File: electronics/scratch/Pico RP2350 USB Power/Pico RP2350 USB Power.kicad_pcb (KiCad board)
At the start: 2 copper layers, 77 x 64 mm, 48 parts, among them J1 RFM69HCW, J10 IR TX AOE, J11 IR RX 1, J12 IR RX 2, J13 IR RX 3, J14 BUTTON A, J15 BUTTON B, J16 LED STRIP 1, J17 LED STRIP 2, J18 LED STRIP 3, J19 LED STRIP 4, J2 SD CARD, J20 LED STRIP 5, J21 LED STRIP 6, J22 POWER, J3 I2C_1, J4 I2C_2, J5 I2C_3, J6 I2C_STEMMA, J7 I2S AMP, J8 IR TX LINE, J9 IR TX CONE, Q1 AO3406, Q2 AO3406, Q3 AO3406, Q4 AO3401A, Q5 C20917, SW1 POWER, U1 74HCT244

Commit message: More pinout labels, removed some component labels, fixed STEMMA MP ground.
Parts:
- J6: value I2C_STEMMA -> STEMMA
- moved J13 3.46 mm to (138.0, 101.0)
- moved J12 2.08 mm to (127.9, 101.0)
- moved J5 2.00 mm to (117.7, 60.0)
- moved J4 1.41 mm to (117.7, 64.0)
- moved D2 1.00 mm to (166.0, 44.0)
- moved R9 1.00 mm to (170.0, 44.0)
- moved J3 0.82 mm to (117.7, 68.0)
- moved J14 0.54 mm to (187.1, 70.0)
- moved J15 0.54 mm to (187.1, 65.0)
- moved J22 0.54 mm to (187.1, 56.0)
- moved J10 0.34 mm to (117.7, 92.0)
- moved J8 0.34 mm to (117.7, 84.0)
- moved J9 0.34 mm to (117.7, 88.0)
- moved J11 0.27 mm to (117.7, 101.0)
- moved ON/OFF 0.10 mm to (179.9, 45.0)
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- renumbered SW1 to ON/OFF
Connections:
- J11 pad 1: +3.3V -> GND
- J11 pad 3: GND -> +3.3V
- J12 pad 1: +3.3V -> GND
- J12 pad 3: GND -> +3.3V
- J13 pad 1: +3.3V -> GND
- J13 pad 3: GND -> +3.3V
- J6 pad MP: (no net) -> GND
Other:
- board size 77 x 64 mm -> 75 x 64 mm
- board text added: "+3v"
- board text added: "+5v"
- board text added: "D"
- board text added: "GND"
- board text added: "SCL"
- board text added: "SDA"

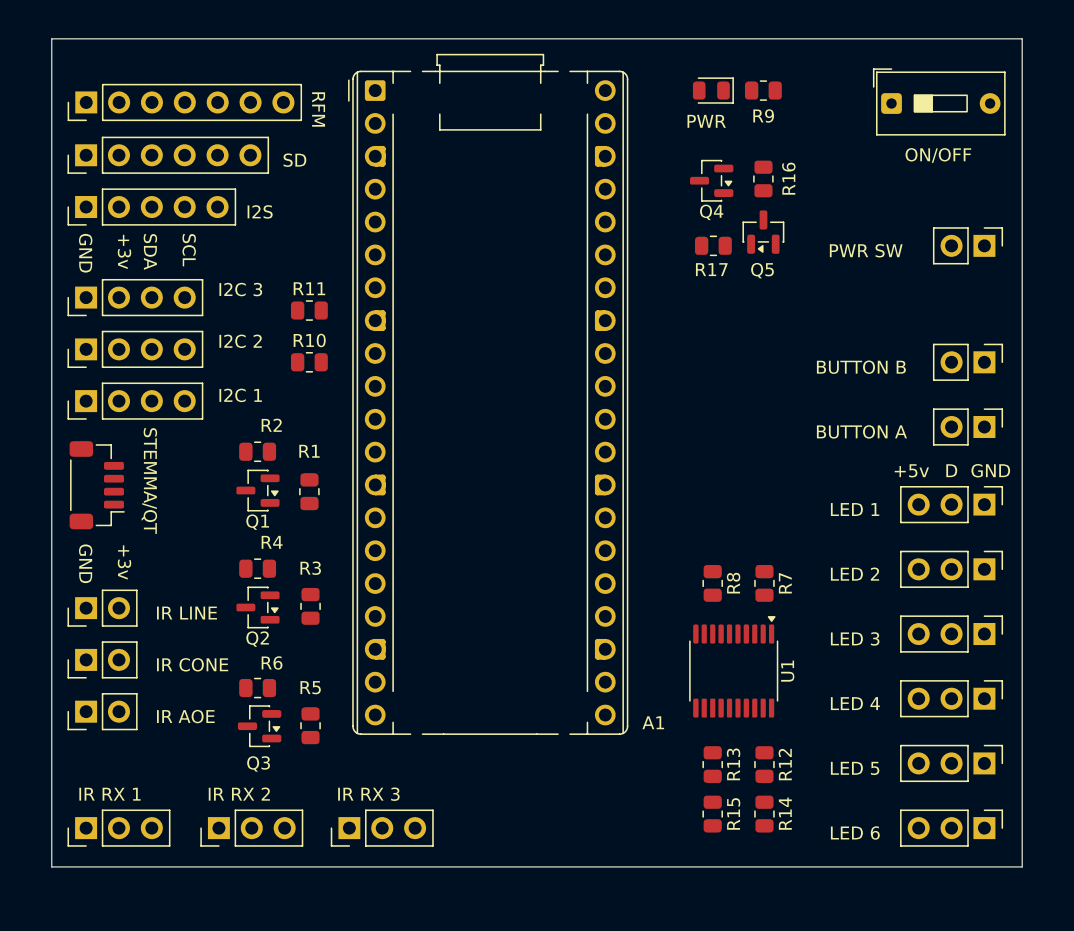
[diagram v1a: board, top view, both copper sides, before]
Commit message: Minor cleanup of USB power main board
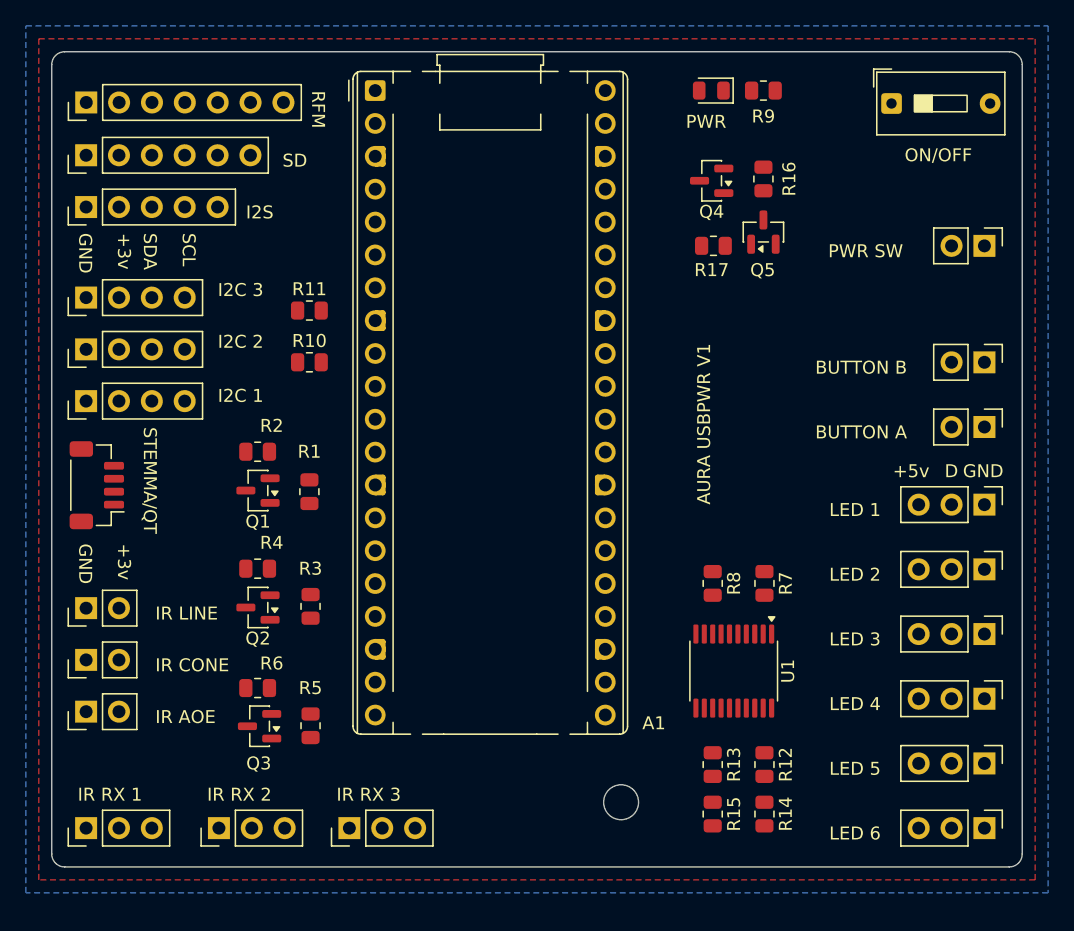
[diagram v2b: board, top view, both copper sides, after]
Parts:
- added REF**: MountingHole_2.7mm_M2.5, MountingHole:MountingHole_2.7mm_M2.5, F.Cu at (159.0, 99.0)
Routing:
- added copper zone on B.Cu, net +3.3V
- added copper zone on F.Cu, net GND
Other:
- board size 75 x 64 mm -> 75 x 63 mm
- board text added: "AURA USBPWR V1"

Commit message: Working on 5V power fills for 3 amps
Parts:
- removed ON/OFF: POWER, Button_Switch_THT:SW_DIP_SPSTx01_Slide_9.78x4.72mm_W7.62mm_P2.54mm
- removed REF**: MountingHole_2.7mm_M2.5, MountingHole:MountingHole_2.7mm_M2.5
- added SW1: POWER, Button_Switch_THT:SW_DIP_SPSTx01_Slide_9.78x4.72mm_W7.62mm_P2.54mm, F.Cu at (179.8, 98.2)
- moved D2 56.7 mm to (175.0, 100.0)
- moved R9 53.7 mm to (175.0, 97.5), turned to 0 degrees
- moved J22 36.2 mm to (187.1, 92.2)
- moved J16 31.0 mm to (187.1, 45.0)
- moved J17 31.0 mm to (187.1, 50.0)
- moved J18 31.0 mm to (187.1, 55.0)
- moved J19 31.0 mm to (187.1, 60.0)
- moved J20 31.0 mm to (187.1, 65.0)
- moved J21 31.0 mm to (187.1, 70.0)
- moved R17 12.7 mm to (171.9, 44.8), turned to -90 degrees
- moved J14 12.0 mm to (187.1, 82.0)
- moved J15 12.0 mm to (187.1, 77.0)
- moved R8 11.3 mm to (170.9, 71.9), turned to 90 degrees
- moved R7 10.7 mm to (166.9, 71.9), turned to 90 degrees
- moved Q5 10.3 mm to (168.7, 44.8), turned to 180 degrees
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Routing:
- net /LED STRIP 1: track 0.00 -> 21.8 mm, vias 0 -> 2
- net /5V_ENABLE: track 0.00 -> 21.0 mm, vias 0 -> 2
- net /LED STRIP 3: track 0.00 -> 17.0 mm
- net /LED STRIP 2: track 0.00 -> 16.4 mm
- net /LED STRIP 4: track 0.00 -> 14.6 mm
- net /LED STRIP 5: track 0.00 -> 12.3 mm
- net /LED STRIP 6: track 0.00 -> 10.9 mm
- net Net-(Q4-G): track 0.00 -> 4.98 mm
- net GND: track 0.00 -> 2.03 mm, vias 0 -> 2
- added copper zone on F.Cu, net +3.3V
- added copper zone on F.Cu, net +5V
- added copper zone on B.Cu, net GND
- added copper zone on F.Cu, net VBUS
- removed copper zone on B.Cu, net +3.3V
- removed copper zone on F.Cu, net GND
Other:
- board text added: "OFF"
- board text added: "ON"
- board text added: "PWR JP"
- board text removed: "PWR SW"

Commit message: Change RP2350 USB power to a 4 layer board
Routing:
- added copper zone on In2.Cu, net +3.3V
- added copper zone on In1.Cu, net GND
- removed copper zone on F.Cu, net +3.3V
- removed copper zone on B.Cu, net GND
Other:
- copper layers 2 -> 4
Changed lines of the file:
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@@
 	(generator_version "10.0")
 	(general
-		(thickness 1.6)
+		(thickness 1.6062)
 		(legacy_teardrops no)
 	)
@@
 	(layers
 		(0 "F.Cu" signal)
+		(4 "In1.Cu" signal)
+		(6 "In2.Cu" signal)
 		(2 "B.Cu" signal)
 		(9 "F.Adhes" user "F.Adhesive")
@@
 			)
 			(layer "dielectric 1"
+				(type "prepreg")
+				(thickness 0.2104)
+				(material "FR4")
+				(epsilon_r 4.4)
+				(loss_tangent 0.02)
+			)
+			(layer "In1.Cu"
+				(type "copper")
+				(thickness 0.0152)
+			)
+			(layer "dielectric 2"
 				(type "core")
-				(thickness 1.51)
+				(thickness 1.065)
 				(material "FR4")
-				(epsilon_r 4.5)
+				(epsilon_r 4.6)
+				(loss_tangent 0.02)
+			)
+			(layer "In2.Cu"
+				(type "copper")
+				(thickness 0.0152)
+			)
+			(layer "dielectric 3"
+				(type "prepreg")
+				(thickness 0.2104)
+				(material "FR4")
+				(epsilon_r 4.4)
 				(loss_tangent 0.02)
 			)
@@
 	)
 	(zone
-		(net "+3.3V")
-		(locked yes)
-		(layer "F.Cu")
+		(net "GND")
+		(layer "In1.Cu")
 		(hatch edge 0.5)
 		(connect_pads
-			(clearance 0.5)
+			(clearance 0)
 		)
 		(min_thickness 0.25)
@@
 		(polygon
 			(pts
-				(xy 114 40) (xy 191 40) (xy 191 105) (xy 114 105)
+				(xy 114.25 40.25) (xy 190.75 40.25) (xy 190.75 104.75) (xy 114 104.75)
 			)
 		)
 	)
 	(zone
-		(net "GND")
-		(locked yes)
-		(layer "B.Cu")
+		(net "+3.3V")
+		(layer "In2.Cu")
 		(hatch edge 0.5)
 		(priority 2)
 		(connect_pads
-			(clearance 0.5)
+			(clearance 0)
 		)
 		(min_thickness 0.25)
@@
 			(thermal_gap 0.5)
 			(thermal_bridge_width 0.5)
-			(smoothing fillet)
-			(radius 1)
 			(island_removal_mode 1)
 		)
 		(polygon
 			(pts
-				(xy 192 39) (xy 192 106) (xy 113 106) (xy 113 39)
+				(xy 114.25 40.25) (xy 190.75 40.25) (xy 190.75 104.75) (xy 114 104.75)
 			)
 		)

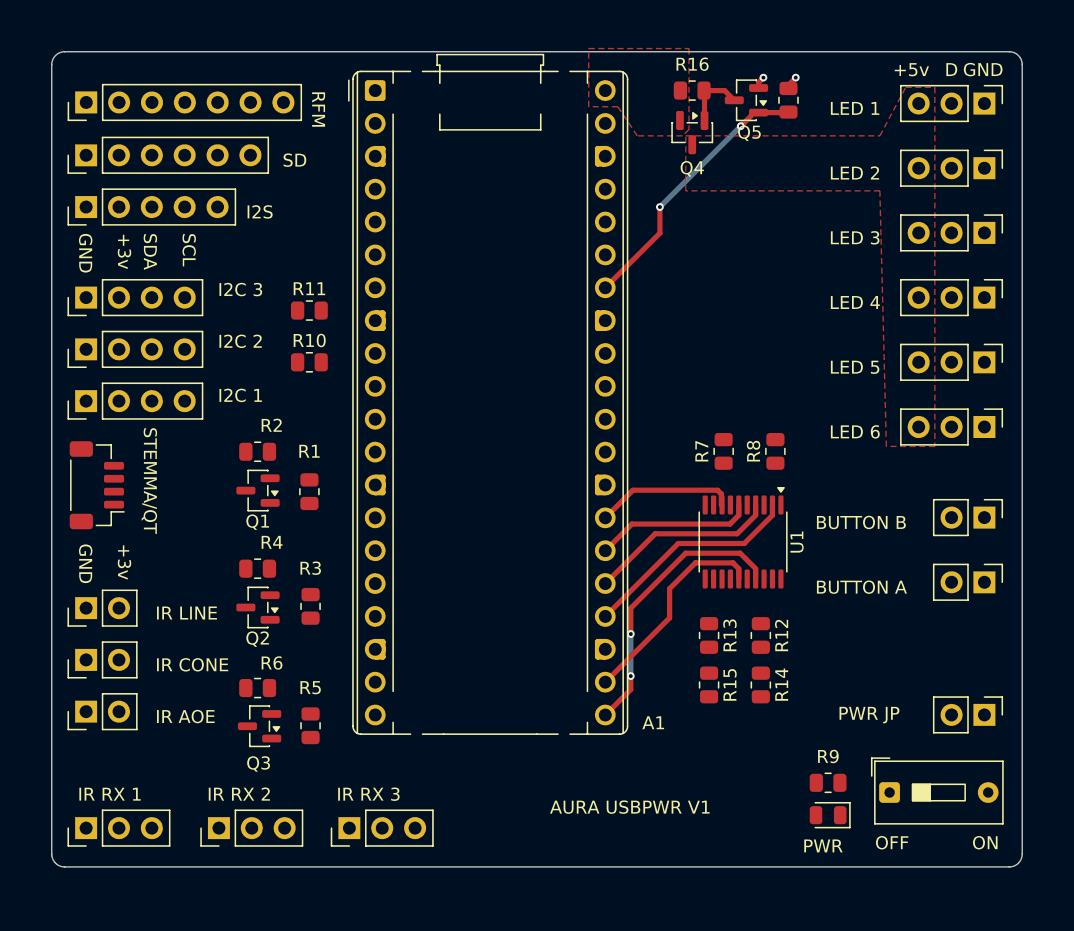
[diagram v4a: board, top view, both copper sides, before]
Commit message: L shaped neopixel pin layout
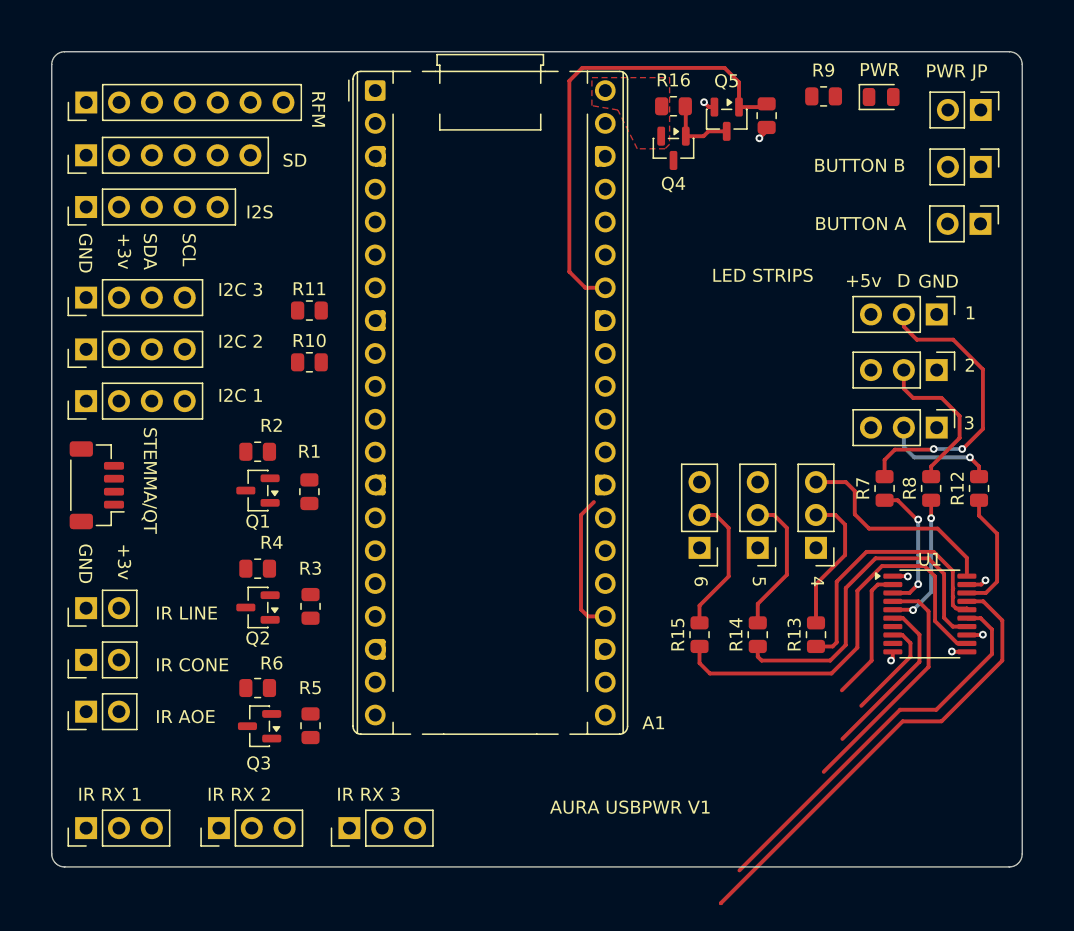
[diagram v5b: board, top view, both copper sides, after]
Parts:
- removed SW1: POWER, Button_Switch_THT:SW_DIP_SPSTx01_Slide_9.78x4.72mm_W7.62mm_P2.54mm
- moved D2 55.7 mm to (179.1, 44.5), turned to 0 degrees
- moved R9 53.1 mm to (174.7, 44.5)
- moved J22 46.8 mm to (186.8, 45.5)
- moved J14 27.7 mm to (186.8, 54.3)
- moved J15 27.1 mm to (186.8, 49.9)
- moved J21 23.9 mm to (165.1, 79.3), turned to 180 degrees
- moved J19 23.3 mm to (174.1, 79.3), turned to 180 degrees
- moved J20 22.6 mm to (169.6, 79.3), turned to 180 degrees
- moved R12 20.3 mm to (186.7, 74.8), turned to 90 degrees
- moved J16 16.7 mm to (183.4, 61.3)
- moved J17 16.0 mm to (183.4, 65.6)
- moved J18 15.5 mm to (183.4, 70.0)
- moved U1 15.5 mm to (182.9, 84.5), turned to 0 degrees
- moved R7 12.8 mm to (179.4, 74.8)
- moved R8 12.4 mm to (183.0, 74.8)
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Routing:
- net /LED SHIFTED 6: track 0.00 -> 32.8 mm
- net /LED SHIFTED 5: track 0.00 -> 27.1 mm
- net Net-(J16-Pin_2): track 0.00 -> 22.9 mm, vias 0 -> 2
- net /LED SHIFTED 4: track 0.00 -> 21.0 mm
- net +5V: track 0.00 -> 16.6 mm
- net /5V_ENABLE: track 21.0 -> 36.2 mm, vias 2 -> 0
- net /LED STRIP 2: track 16.4 -> 30.6 mm
- net /LED STRIP 1: track 21.8 -> 36.0 mm, vias 2 -> 0
- net Net-(J17-Pin_2): track 0.00 -> 12.2 mm
- net Net-(J19-Pin_2): track 0.00 -> 11.1 mm
- net Net-(J21-Pin_2): track 0.00 -> 10.9 mm
- net Net-(J20-Pin_2): track 0.00 -> 10.9 mm
- net /LED SHIFTED 2: track 0.00 -> 10.6 mm, vias 0 -> 2
- net /LED SHIFTED 1: track 0.00 -> 10.5 mm, vias 0 -> 2
- net /LED SHIFTED 3: track 0.00 -> 9.57 mm
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- removed copper zone on F.Cu, net +5V
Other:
- board text added: "1"
- board text added: "2"
- board text added: "3"
- board text added: "4"
- board text added: "5"
- board text added: "6"
- board text added: "LED STRIPS"
- board text removed: "LED 1"
- board text removed: "LED 2"
- board text removed: "LED 3"
- board text removed: "LED 4"
- board text removed: "LED 5"
- board text removed: "LED 6"
- board text removed: "OFF"
- board text removed: "ON"

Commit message: All traces for RP2350 USB power except GND and 3.3v
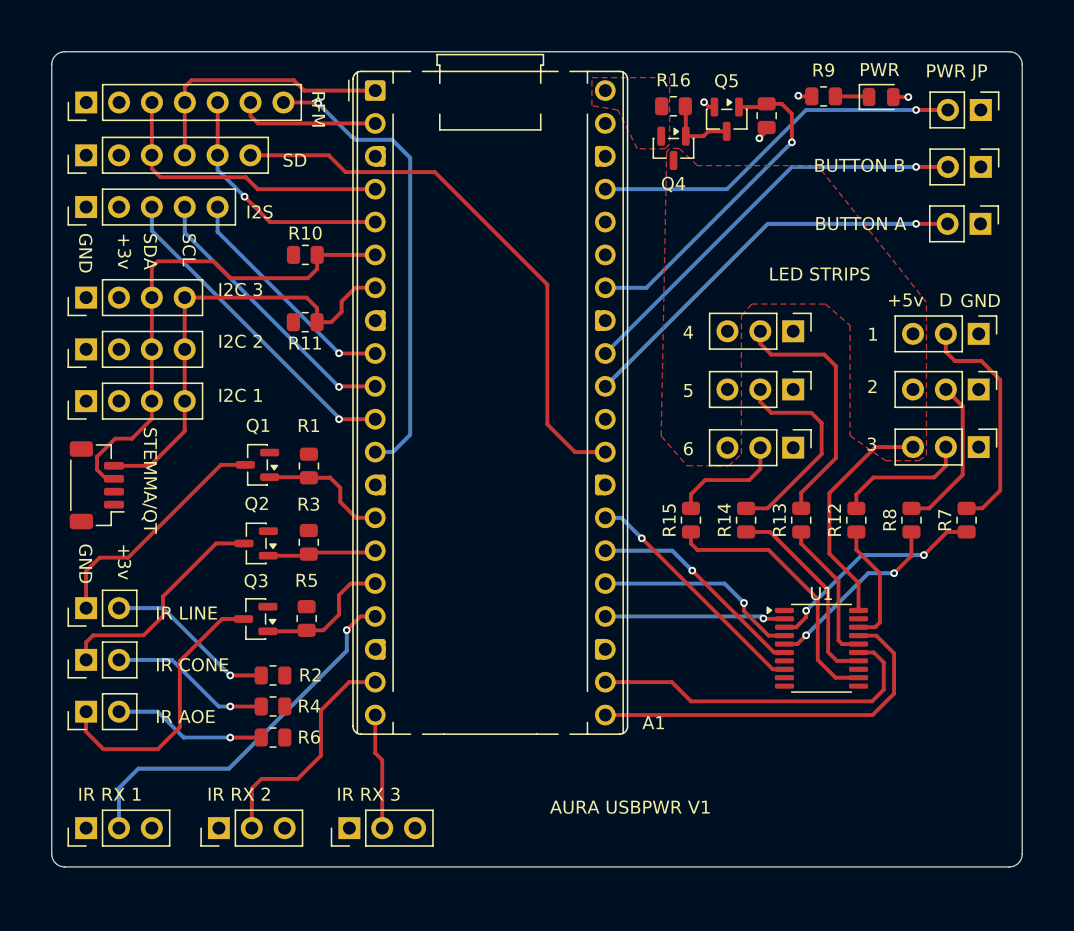
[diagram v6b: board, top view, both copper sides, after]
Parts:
- moved R2 17.3 mm to (132.1, 89.2)
- moved J19 16.8 mm to (172.3, 62.6), turned to -90 degrees
- moved J20 12.5 mm to (172.3, 67.1), turned to -90 degrees
- moved R4 10.7 mm to (132.1, 91.6)
- moved J21 10.6 mm to (172.3, 71.6), turned to -90 degrees
- moved R12 9.79 mm to (177.2, 77.2)
- moved R13 8.92 mm to (172.9, 77.2)
- moved R14 8.90 mm to (168.7, 77.2)
- moved R15 8.87 mm to (164.4, 77.2)
- moved U1 8.78 mm to (174.5, 87.1)
- moved R10 8.31 mm to (134.6, 56.7)
- moved R5 8.29 mm to (134.7, 84.8)
- moved Q3 8.29 mm to (130.8, 84.8)
- moved R7 6.79 mm to (185.7, 77.2)
- moved Q2 4.95 mm to (130.8, 79.0)
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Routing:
- net /SD CARD CS: track 0.00 -> 43.3 mm
- net /SDA: track 0.00 -> 39.1 mm
- net /RFM69 Reset: track 0.00 -> 36.2 mm, vias 0 -> 1
- net /SCL: track 0.00 -> 34.6 mm
- net /BUTTON B: track 0.00 -> 32.5 mm, vias 0 -> 1
- net /BUTTON A: track 0.00 -> 31.7 mm, vias 0 -> 1
- net /IR RX 1: track 0.00 -> 29.3 mm, vias 0 -> 1
- net /3V3_EN: track 0.00 -> 29.0 mm, vias 0 -> 1
- net /I2S LRC: track 0.00 -> 25.2 mm, vias 0 -> 1
- net /SCLK: track 0.00 -> 23.0 mm
- net /I2S BCLK: track 0.00 -> 21.7 mm, vias 0 -> 1
- net Net-(J10-Pin_1): track 0.00 -> 21.4 mm
- net /MISO: track 0.00 -> 20.5 mm
- net /MOSI: track 0.00 -> 19.1 mm, vias 0 -> 1
- net Net-(J8-Pin_1): track 0.00 -> 18.6 mm
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- added copper zone on F.Cu, net +5V

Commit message: Ground and 3.3v traces, board complete (I think)
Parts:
- moved J19 0.20 mm to (172.3, 62.8)
- moved R5 0.18 mm to (134.9, 84.8)
- moved Q3 0.14 mm to (130.9, 84.8)
- moved Q2 0.10 mm to (130.9, 79.0)
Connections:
- A1 pad 33: GNDA -> GND
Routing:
- net GND: track 3.08 -> 31.1 mm, vias 3 -> 26
- net +3.3V: track 1.16 -> 15.1 mm, vias 1 -> 11
- net /LED STRIP 1: track 29.4 -> 30.9 mm
- net /LED STRIP 2: track 26.9 -> 28.2 mm
- net /LED SHIFTED 3: track 9.55 -> 10.3 mm
